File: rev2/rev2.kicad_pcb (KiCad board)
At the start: 4 copper layers, 49.5 x 49.8 mm, 52 parts, among them J1 Termination, J10 GPIO, J2 CAN1, J3 Termination, J4 CAN2, J5 SWD ASYNC, J6 LIN Pots, J7 AIN, J8 USB_OTG, J9 PWR_USB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

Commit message: did like a quarter of the routing
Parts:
- moved U6 38.6 mm to (149.2, 103.0), turned to 90 degrees
- moved C28 35.3 mm to (154.7, 90.7), turned to 180 degrees
- moved C43 33.0 mm to (143.0, 112.5), turned to -90 degrees
- moved J1 6.84 mm to (157.0, 79.3), turned to 0 degrees
- moved C48 5.11 mm to (120.9, 108.0), turned to 90 degrees
- moved C49 5.11 mm to (119.4, 108.0), turned to 90 degrees
- moved R5 4.55 mm to (155.8, 115.2), turned to -90 degrees
- moved J3 4.49 mm to (156.8, 121.3)
- moved C24 1.96 mm to (138.8, 83.8)
- moved C47 1.78 mm to (119.4, 104.6), turned to -90 degrees
- moved C39 1.78 mm to (120.9, 104.6), turned to -90 degrees
- moved R4 1.73 mm to (157.2, 83.5), turned to 0 degrees
- moved R7 1.55 mm to (118.6, 110.7)
- moved J4 1.42 mm to (150.3, 119.0)
- moved C21 1.02 mm to (141.5, 112.5)
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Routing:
- net GND: track 9.14 -> 83.0 mm, vias 0 -> 26
- net +3.3V: track 10.7 -> 64.3 mm, vias 0 -> 16
- net /STMPS2151STR_FAULT: track 0.00 -> 34.2 mm, vias 0 -> 2
- net /STMPS2151STR_EN: track 0.00 -> 33.4 mm, vias 0 -> 2
- net +5V: track 0.00 -> 31.7 mm, vias 0 -> 4
- net /CAN2-: track 7.52 -> 29.1 mm
- net /CAN1+: track 6.64 -> 25.9 mm
- net /CAN2+: track 7.88 -> 26.3 mm
- net /CAN1-: track 7.00 -> 25.2 mm
- net /Silent Mode 2: track 0.00 -> 14.3 mm
- net CAN2_TX: track 0.00 -> 12.0 mm
- net CAN1_RX: track 0.00 -> 11.3 mm
- net CAN1_TX: track 0.00 -> 7.47 mm
- net Net-(U1-VCAP_2): track 0.00 -> 5.38 mm
- net CAN2_RX: track 0.00 -> 2.42 mm
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
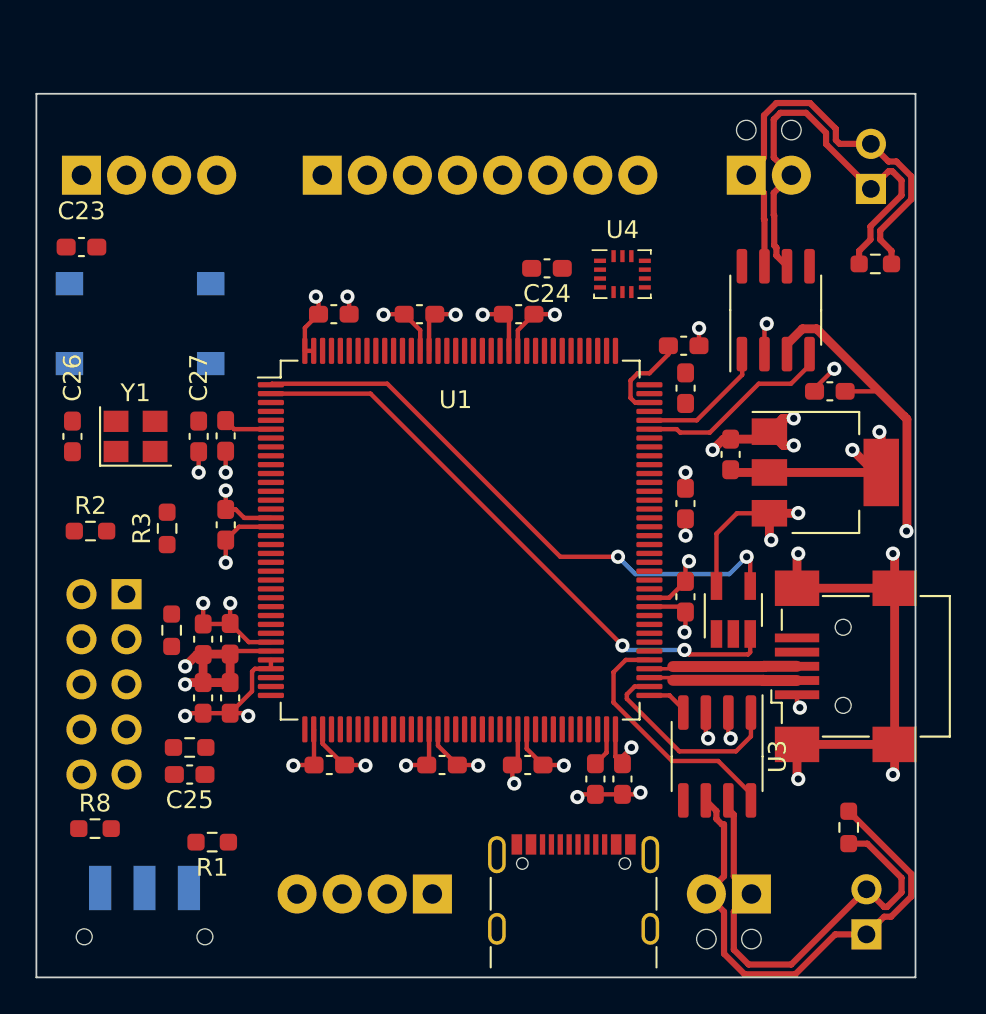
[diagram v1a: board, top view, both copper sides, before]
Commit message: finished the pcb routing except the usb C now I just need to do the DRC
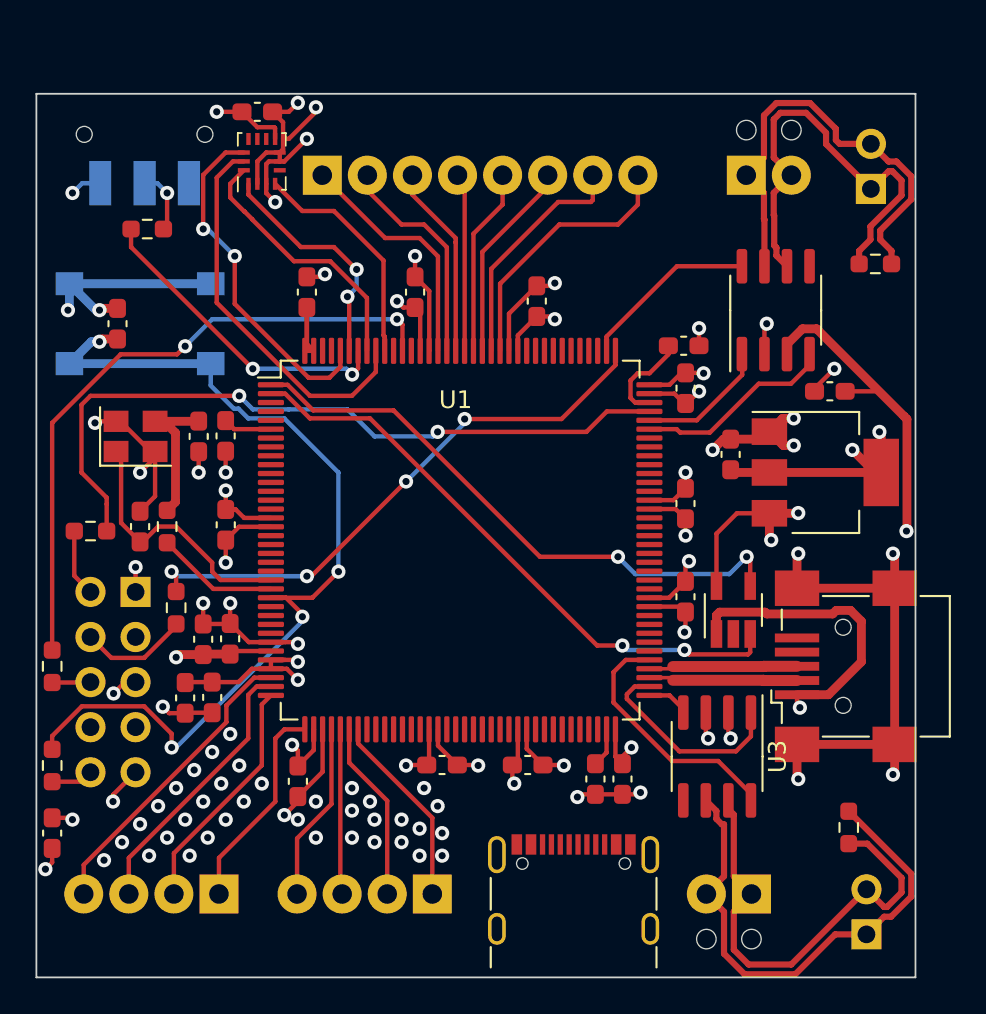
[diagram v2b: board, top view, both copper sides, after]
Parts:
- moved SW2 45.2 mm to (116.1, 76.2), turned to 0 degrees
- moved J6 41.2 mm to (120.3, 119.0), turned to 180 degrees
- moved R1 34.7 mm to (116.2, 81.5), turned to 0 degrees
- moved U4 21.3 mm to (122.7, 77.7), turned to 90 degrees
- moved C24 18.6 mm to (122.4, 74.9)
- moved R7 9.00 mm to (110.9, 106.2), turned to 90 degrees
- moved C25 8.42 mm to (110.9, 115.6), turned to -90 degrees
- moved C26 6.35 mm to (115.8, 98.3)
- moved C23 4.77 mm to (114.6, 86.9), turned to 90 degrees
- moved R8 4.30 mm to (110.9, 111.8), turned to 90 degrees
- moved C48 2.53 mm to (118.4, 108.0), turned to -90 degrees
- moved C42 2.00 mm to (124.7, 112.6), turned to 90 degrees
- moved C32 1.96 mm to (125.2, 85.1), turned to 90 degrees
- moved R6 1.30 mm to (117.9, 102.9)
- moved C45 1.27 mm to (131.3, 85.1), turned to 90 degrees
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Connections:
- J10 pad 1: GPIO8 -> GPIO6
- J10 pad 2: GPIO7 -> GPIO5
- J10 pad 3: Net-(J10-Pin_3) -> GPIO4
- J10 pad 4: Net-(J10-Pin_4) -> GPIO3
- J10 pad 5: Net-(J10-Pin_5) -> GPIO2
- J10 pad 6: Net-(J10-Pin_6) -> GPIO1
- J10 pad 7: Net-(J10-Pin_7) -> GPIO8
- J10 pad 8: Net-(J10-Pin_8) -> GPIO7
- J6 pad 1: Net-(J6-Pin_1) -> linpot4
- J6 pad 2: Net-(J6-Pin_2) -> linpot3
- J6 pad 3: Net-(J6-Pin_3) -> linpot2
- J6 pad 4: Net-(J6-Pin_4) -> linpot1
- J7 pad 1: Net-(J7-Pin_1) -> A4
- J7 pad 2: Net-(J7-Pin_2) -> A3
- J7 pad 3: Net-(J7-Pin_3) -> A2
- J7 pad 4: Net-(J7-Pin_4) -> A1
- U1 pad 124: Net-(J10-Pin_8) -> GPIO1
- U1 pad 125: Net-(J10-Pin_7) -> GPIO2
- U1 pad 126: Net-(J10-Pin_6) -> GPIO3
- U1 pad 127: Net-(J10-Pin_5) -> GPIO4
- U1 pad 128: Net-(J10-Pin_4) -> GPIO5
- U1 pad 129: Net-(J10-Pin_3) -> GPIO6
- U1 pad 34: Net-(J6-Pin_1) -> linpot1
- U1 pad 35: Net-(J6-Pin_2) -> linpot2
- U1 pad 36: Net-(J6-Pin_3) -> linpot3
- U1 pad 37: Net-(J6-Pin_4) -> linpot4
- U1 pad 40: Net-(J7-Pin_1) -> A1
- U1 pad 41: Net-(J7-Pin_2) -> A2
- U1 pad 42: Net-(J7-Pin_3) -> A3
- U1 pad 43: Net-(J7-Pin_4) -> A4
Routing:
- net NRST: track 0.00 -> 54.2 mm, vias 0 -> 4
- net GND: track 83.0 -> 131.7 mm, vias 26 -> 74
- net SYS_JTMS_SWDIO: track 0.00 -> 41.4 mm, vias 0 -> 2
- net SYS_JTDO_SWO: track 0.00 -> 36.6 mm, vias 0 -> 2
- net SYS_JTCK_SWCLK: track 0.00 -> 32.2 mm, vias 0 -> 4
- net +3.3V: track 64.3 -> 87.6 mm, vias 16 -> 21
- net /LSM_SCL: track 0.00 -> 21.8 mm
- net /LSM_CS: track 0.00 -> 19.8 mm, vias 0 -> 2
- net BOOT0: track 0.00 -> 17.9 mm, vias 0 -> 2
- net linpot1: track 0.00 -> 17.7 mm
- net /VBUS1: track 0.79 -> 17.1 mm
- net linpot2: track 0.00 -> 15.5 mm
- net /HSE_IN: track 0.00 -> 15.1 mm
- net GPIO7: track 0.00 -> 15.0 mm
- net /LSM_SDA: track 0.00 -> 14.9 mm
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
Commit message: added finishing touches to the rev 2 design
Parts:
- SW2: footprint Button_Switch_SMD:SW_SPDT_CK-JS102011SAQN -> Button_Switch_SMD:SW_SPDT_PCM12
- moved R4 0.95 mm to (157.2, 82.5), turned to -90 degrees
- moved C49 0.06 mm to (119.8, 108.0)
- moved J9 0.06 mm to (140.2, 119.9)
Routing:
- net GND: track 131.7 -> 167.6 mm, vias 74 -> 53
- net +3.3V: track 87.6 -> 91.4 mm, vias 21 -> 23
- net /CAN2+: track 26.3 -> 29.8 mm
- net +5V: track 31.7 -> 34.6 mm, vias 4 -> 6
- net /CAN2-: track 29.1 -> 31.5 mm
- net /CAN1+: track 25.9 -> 28.2 mm
- net /CAN1-: track 25.2 -> 23.0 mm
- net /VBUS1: track 17.1 -> 18.5 mm
- net Net-(SW2-B): track 3.62 -> 4.71 mm
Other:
- board size 49.5 x 49.8 mm -> 49.9 x 49.8 mm

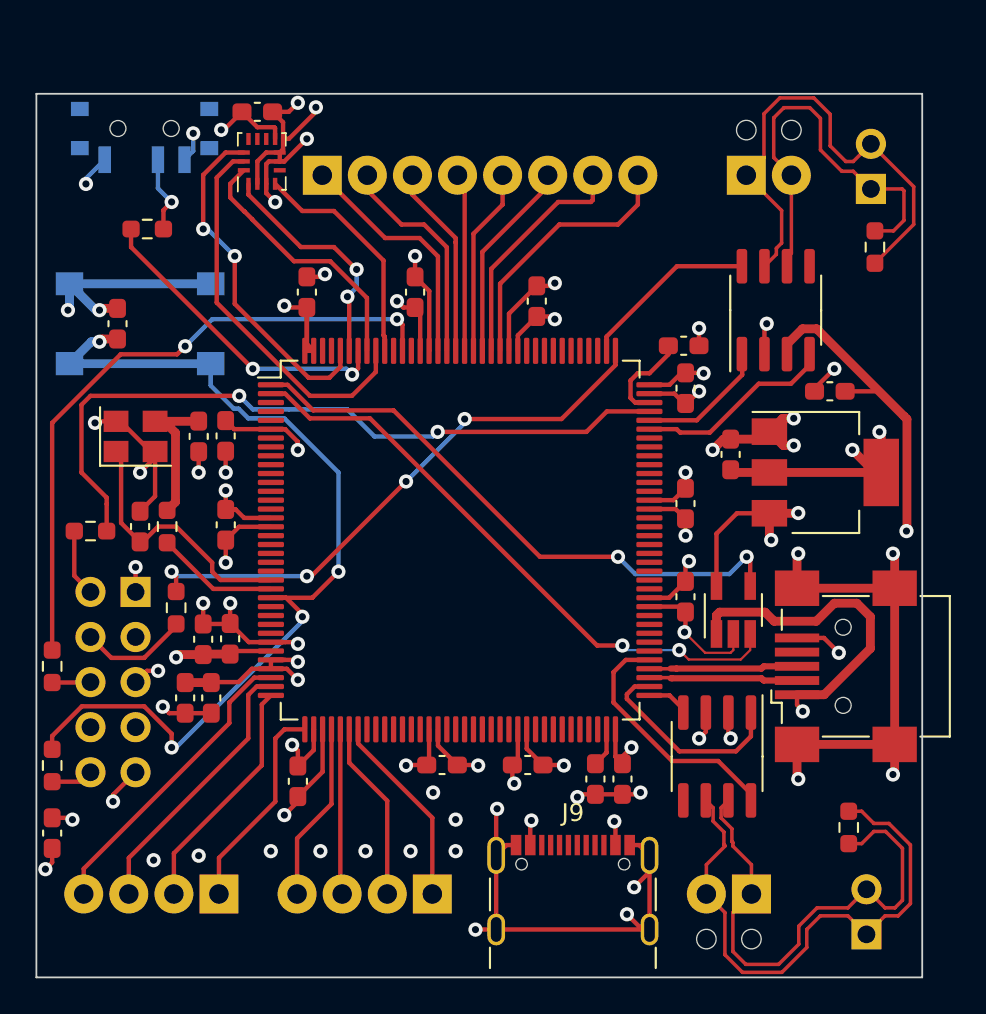
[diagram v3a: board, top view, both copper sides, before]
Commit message: added some silkscreen to to differentiate parts
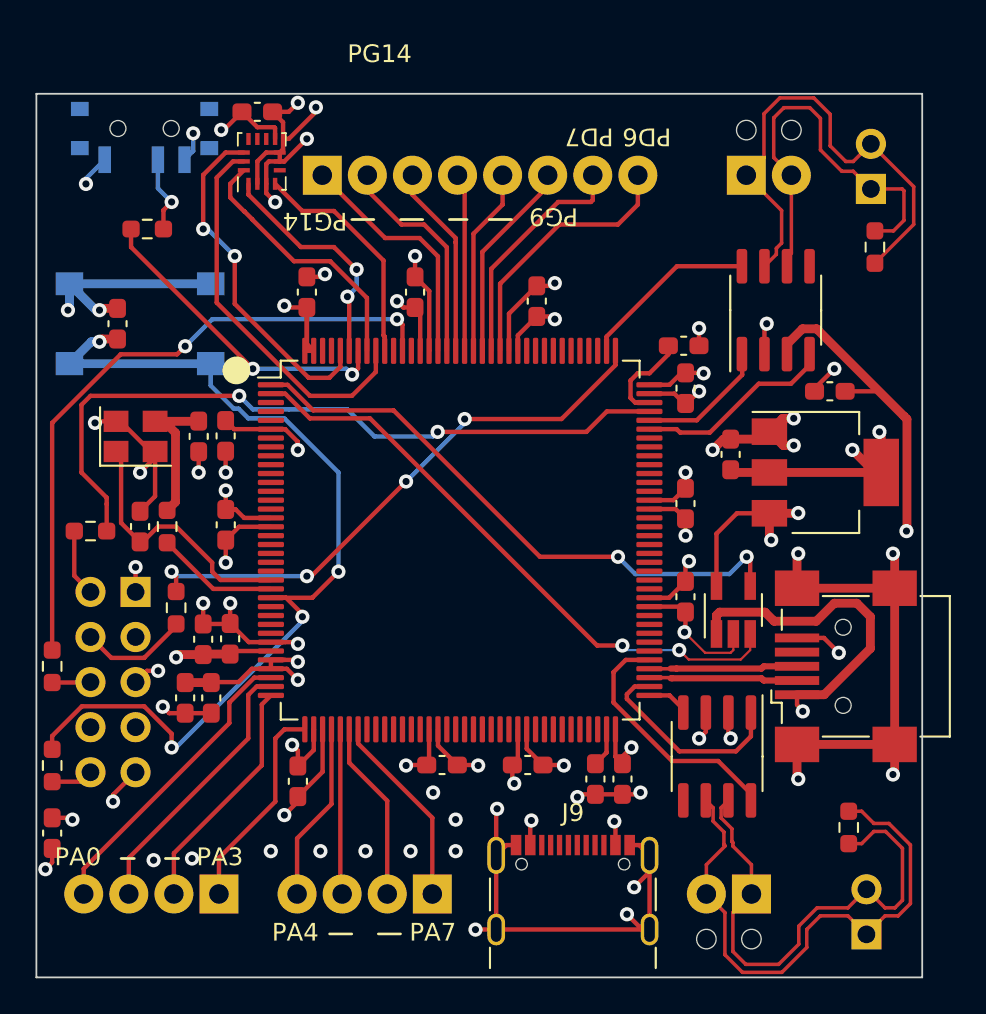
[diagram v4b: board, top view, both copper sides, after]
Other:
- board text added: "120"
- board text added: "2"
- board text added: "Analog Pin"
- board text added: "CAN"
- board text added: "GPIO"
- board text added: "LIN Pots"
- board text added: "PA0"
- board text added: "PA3"
- board text added: "PA4"
- board text added: "PA7"
- board text added: "PD6"
- board text added: "PD7"
- board text added: "PG14"
- board text added: "PG9"
- board text added: "RST"
- board text added: "SWD"
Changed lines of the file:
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@@
     (property "ki_keywords" "switch single-pole double-throw spdt ON-ON")
     (attr smd)
-    (fp_text reference "SW2" (at 0 3.2 180) (layer "B.SilkS")
+    (fp_text reference "SW2" (at -0.078 3.2) (layer "B.SilkS")
         (effects (font (size 1 1) (thickness 0.15)) (justify mirror))
     )
@@
     )
   )
+  (gr_circle (center 117.5 101.75) (end 117.75 102)
+    (stroke (width 0.15) (type default)) (fill none) (layer "B.SilkS"))
+  (gr_line (start 130.5 81) (end 131.75 81)
+    (stroke (width 0.15) (type default)) (layer "F.SilkS"))
+  (gr_line (start 135.5 81) (end 136.75 81)
+    (stroke (width 0.15) (type default)) (layer "F.SilkS"))
+  (gr_line (start 126.5 121.25) (end 127.75 121.25)
+    (stroke (width 0.15) (type default)) (layer "F.SilkS"))
+  (gr_line (start 133.25 81) (end 134.25 81)
+    (stroke (width 0.15) (type default)) (layer "F.SilkS"))
+  (gr_circle (center 121.25 89.5) (end 121.957107 89.5)
+    (stroke (width 0.15) (type solid)) (fill solid) (layer "F.SilkS"))
+  (gr_line (start 129.25 121.25) (end 130.5 121.25)
+    (stroke (width 0.15) (type default)) (layer "F.SilkS"))
+  (gr_line (start 127.75 81) (end 129 81)
+    (stroke (width 0.15) (type default)) (layer "F.SilkS"))
+  (gr_line (start 114.75 117) (end 115.5 117)
+    (stroke (width 0.15) (type default)) (layer "F.SilkS"))
+  (gr_line (start 117.25 117) (end 118 117)
+    (stroke (width 0.15) (type default)) (layer "F.SilkS"))
   (gr_rect (start 109.982 73.914) (end 159.893 123.698)
     (stroke (width 0.1) (type default)) (fill none) (layer "Edge.Cuts"))
+  (gr_text "LIN Pots" (at 119.25 115.25) (layer "B.SilkS")
+    (effects (font (size 1 1) (thickness 0.15)) (justify left bottom mirror))
+  )
+  (gr_text "CAN" (at 150.5 115.25) (layer "B.SilkS")
+    (effects (font (size 1 1) (thickness 0.15)) (justify left bottom mirror))
+  )
+  (gr_text "GPIO" (at 132.75 82.25 180) (layer "B.SilkS")
+    (effects (font (size 1 1) (thickness 0.15)) (justify left bottom mirror))
+  )
+  (gr_text "RST" (at 117.25 83.5) (layer "B.SilkS")
+    (effects (font (size 1 1) (thickness 0.15)) (justify left bottom mirror))
+  )
+  (gr_text "SWD" (at 116 100.25) (layer "B.SilkS")
+    (effects (font (size 1 1) (thickness 0.15)) (justify left bottom mirror))
+  )
+  (gr_text "Analog Pin" (at 132.5 115.25) (layer "B.SilkS")
+    (effects (font (size 1 1) (thickness 0.15)) (justify left bottom mirror))
+  )
+  (gr_text "120" (at 158.5 79.5 -90) (layer "B.SilkS")
+    (effects (font (size 1 1) (thickness 0.15)) (justify left bottom mirror))
+  )
+  (gr_text "120 " (at 158.5 121.25 -90) (layer "B.SilkS")
+    (effects (font (size 1 1) (thickness 0.15)) (justify left bottom mirror))
+  )
+  (gr_text "CAN\n" (at 150 82 180) (layer "B.SilkS")
+    (effects (font (size 1 1) (thickness 0.15)) (justify left bottom mirror))
+  )
+  (gr_text "2" (at 111.75 102.5) (layer "B.SilkS")
+    (effects (font (size 1 1) (thickness 0.15)) (justify left bottom mirror))
+  )
+  (gr_text "PG14" (at 127.5 72.25) (layer "F.SilkS")
+    (effects (font (size 1 1) (thickness 0.15)) (justify left bottom))
+  )
+  (gr_text "PD7\n" (at 142.5 75.75 180) (layer "F.SilkS")
+    (effects (font (size 1 1) (thickness 0.15)) (justify left bottom))
+  )
+  (gr_text "PD6" (at 145.75 75.75 180) (layer "F.SilkS")
+    (effects (font (size 1 1) (thickness 0.15)) (justify left bottom))
+  )
+  (gr_text "PA7\n" (at 131 121.75) (layer "F.SilkS")
+    (effects (font (size 1 1) (thickness 0.15)) (justify left bottom))
+  )
+  (gr_text "PA3" (at 119 117.5) (layer "F.SilkS")
+    (effects (font (size 1 1) (thickness 0.15)) (justify left bottom))
+  )
+  (gr_text "PA4" (at 123.25 121.75) (layer "F.SilkS")
+    (effects (font (size 1 1) (thickness 0.15)) (justify left bottom))
+  )
+  (gr_text "PG9" (at 140.5 80.25 180) (layer "F.SilkS")
+    (effects (font (size 1 1) (thickness 0.15)) (justify left bottom))
+  )
+  (gr_text "PA0" (at 111 117.5) (layer "F.SilkS")
+    (effects (font (size 1 1) (thickness 0.15)) (justify left bottom))
+  )
+  (gr_text "PG14" (at 127.5 80.5 180) (layer "F.SilkS")
+    (effects (font (size 1 1) (thickness 0.15)) (justify left bottom))
+  )
   (dimension (type aligned) (layer "Dwgs.User")
     (pts (xy 109.982 73.914) (xy 109.982 123.698))
@@
   (via (at 123.19 116.586) (size 0.8) (drill 0.4) (layers "F.Cu" "B.Cu") (net 2))
   (via (at 152.908 99.822) (size 0.8) (drill 0.4) (layers "F.Cu" "B.Cu") (net 2))
-  (via (at 119.126 116.84) (size 0.8) (drill 0.4) (layers "F.Cu" "B.Cu") (net 2))
+  (via (at 118.75 117) (size 0.8) (drill 0.4) (layers "F.Cu" "B.Cu") (net 2))
   (via (at 113.284 92.456) (size 0.8) (drill 0.4) (layers "F.Cu" "B.Cu") (net 2))
   (via (at 125.73 74.676) (size 0.8) (drill 0.4) (layers "F.Cu" "B.Cu") (net 2))

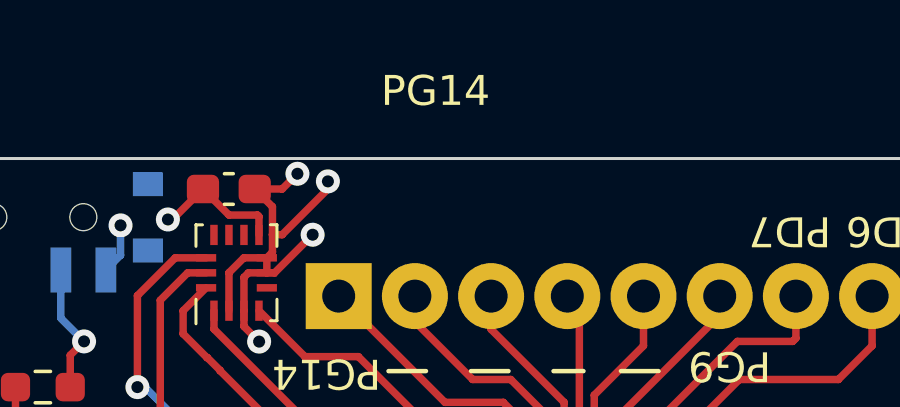
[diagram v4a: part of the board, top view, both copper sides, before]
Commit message: added the most important part, Cat silkscreen. Also added DFR logo,revision number, and the todays date( even though this was finished a while ago)
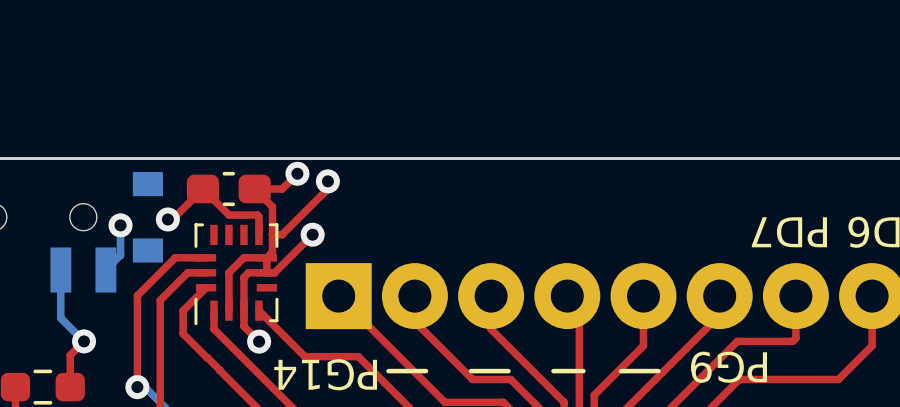
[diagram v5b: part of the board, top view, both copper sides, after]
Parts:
- added G***: LOGO, LOGO, B.Cu at (133.9, 99.1)
- added G***: LOGO, LOGO, B.Cu at (153.8, 93.2)
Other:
- board text added: "REV 2 3/14/24"
